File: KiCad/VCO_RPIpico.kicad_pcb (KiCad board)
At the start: 2 copper layers, 138 x 83 mm, 92 parts, among them J1 AudioJack, J2 Power Jack, SW1 LFO1/2, SW2 Select LFO WaveForm, SW3 Fire4, SW4 Fire3, SW5 Fire2, SW6 Fire1, SW7 Shift2/Save, SW8 Shift1 / Select Bank, U2 PT2399, U3 L7805, sw10 sw_led_fire2, sw11 sw_led_fire3, sw12 sw_led_fire4, sw9 sw_led_fire1

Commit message: KiCad: Schaltplan angepasst
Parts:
- removed R1: 1k, Resistor_SMD:R_1206_3216Metric
- removed R13, R14, R15: 100k, Potentiometer_THT:Potentiometer_Alps_RK09K_Single_Vertical
- added C24: 220n, Capacitor_SMD:C_1206_3216Metric, B.Cu at (103.0, 70.3)
- added R30: 10k, Resistor_SMD:R_1206_3216Metric, F.Cu at (135.0, 39.8)
- added RV1: 10k, poti_alps:Potentiometer_Alps_RK09K_Single_Vertical, F.Cu at (54.5, 71.5)
- added RV2: 10k, poti_alps:Potentiometer_Alps_RK09K_Single_Vertical, F.Cu at (54.5, 101.5)
- added RV3: 10k, poti_alps:Potentiometer_Alps_RK09K_Single_Vertical, F.Cu at (90.5, 101.5)
- C13: value 82nF -> 68nF
- J1: value AudioJack -> AudioJack3_Ground; footprint Connector_Audio:Jack_3.5mm_Ledino_KB3SPRS_Horizontal -> Audiosockets:Jack_3.5mm_Ledino_KB3SPRS_Horizontal
- R19: value 10k -> 4,7k
- RV4, RV5: footprint Potentiometer_THT:Potentiometer_Alps_RK09K_Single_Vertical -> poti_alps:Potentiometer_Alps_RK09K_Single_Vertical
- RV6: value 100k -> 50k; footprint Potentiometer_THT:Potentiometer_Alps_RK09K_Single_Vertical -> poti_alps:Potentiometer_Alps_RK09K_Single_Vertical
- moved R28 18.8 mm to (97.9, 41.1)
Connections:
- J1 pad R: (no net) -> Net-(J1-PadR)
- J1 pad S: Net-(J1-PadS) -> GND
- J1 pad T: GND -> Net-(J1-PadT)
- RV6 pad 2: Net-(J1-PadS) -> Net-(J1-PadT)
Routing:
- net Net-(J1-PadS): track 28.6 -> 0.00 mm
- net Net-(J1-PadT): track 0.00 -> 25.8 mm
- net Net-(C21-Pad2): track 97.9 -> 79.3 mm
- net +3V3: track 103.3 -> 85.1 mm
- net Net-(R5-Pad2): track 14.9 -> 0.00 mm
- net Net-(R4-Pad2): track 14.9 -> 0.10 mm
- net GND: track 145.4 -> 133.0 mm
- net Net-(R28-Pad1): track 12.2 -> 0.00 mm, vias 1 -> 0
- net Net-(C17-Pad2): track 78.7 -> 73.4 mm, vias 2 -> 1
- net Net-(R19-Pad1): track 5.15 -> 0.00 mm
- net Net-(R6-Pad2): track 3.01 -> 0.00 mm
- net Net-(C23-Pad2): track 3.67 -> 1.27 mm

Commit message: KiCad änderungen
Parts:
- removed D12, D16: LED Fire1, LED_SMD:LED_1206_3216Metric
- removed D13, D17: LED Fire2, LED_SMD:LED_1206_3216Metric
- removed D14, D18: LED Fire3, LED_SMD:LED_1206_3216Metric
- removed D15, D19: LED Fire4, LED_SMD:LED_1206_3216Metric
- removed sw10: sw_led_fire2, switches:Multimec Switch THT
- removed sw11: sw_led_fire3, switches:Multimec Switch THT
- removed sw12: sw_led_fire4, switches:Multimec Switch THT
- removed sw9: sw_led_fire1, switches:Multimec Switch THT
- D1: value LED LFO2 -> LED LFO2 yel
- D2: value LED LFO1 -> LED LFO1 yel
- D3: value LED Shift1 -> LED Shift1 yel
- D4: value LED Fire1 -> LED Fire1 blu
- D5: value LED Fire2 -> LED Fire2 blu
- D6: value LED Fire3 -> LED Fire3 blu
- D7: value LED Fire4 -> LED Fire4 blu
- D9: value LED Shift2 -> LED Save red
- J1: footprint Audiosockets:Jack_3.5mm_Ledino_KB3SPRS_Horizontal -> Connector_Audio:Jack_6.35mm_Neutrik_NMJ6HFD2_Horizontal
- R30: moved to B.Cu
- moved D20 49.8 mm to (165.0, 52.6), turned to 0 degrees
- moved R30 47.9 mm to (174.5, 67.0), turned to 180 degrees
- moved J1 47.1 mm to (103.9, 73.9), turned to 90 degrees
- moved R28 42.8 mm to (130.6, 68.8)
- moved RV4 36.0 mm to (90.5, 71.5)
- moved RV5 36.0 mm to (126.5, 71.5)
- moved J2 35.9 mm to (153.2, 61.8)
- moved C10 12.6 mm to (122.7, 53.6)
- moved C24 3.98 mm to (99.8, 72.7), turned to 90 degrees
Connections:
- RV4 pad 2: GND -> Net-(R19-Pad1)
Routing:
- net +5C: track 141.0 -> 79.4 mm
- net Net-(C17-Pad2): track 73.4 -> 38.4 mm
- net Net-(C21-Pad2): track 79.3 -> 45.7 mm
- net /Wave_out: track 82.2 -> 52.1 mm, vias 2 -> 1
- net /led_fire1: track 26.3 -> 2.29 mm
- net /led_fire2: track 26.8 -> 3.06 mm
- net +3V3: track 85.1 -> 63.1 mm
- net Net-(J1-PadT): track 25.8 -> 10.5 mm
- net Net-(D20-K): track 30.0 -> 18.1 mm
- net /led_fire3: track 27.8 -> 19.9 mm
- net Net-(A1-GPIO5): track 19.8 -> 14.5 mm
- net Net-(D20-A): track 5.27 -> 0.00 mm
- net /sw_fire1: track 40.8 -> 38.6 mm
- net /sw_fire2: track 54.3 -> 52.1 mm
- net /sw_fire3: track 92.5 -> 90.3 mm
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
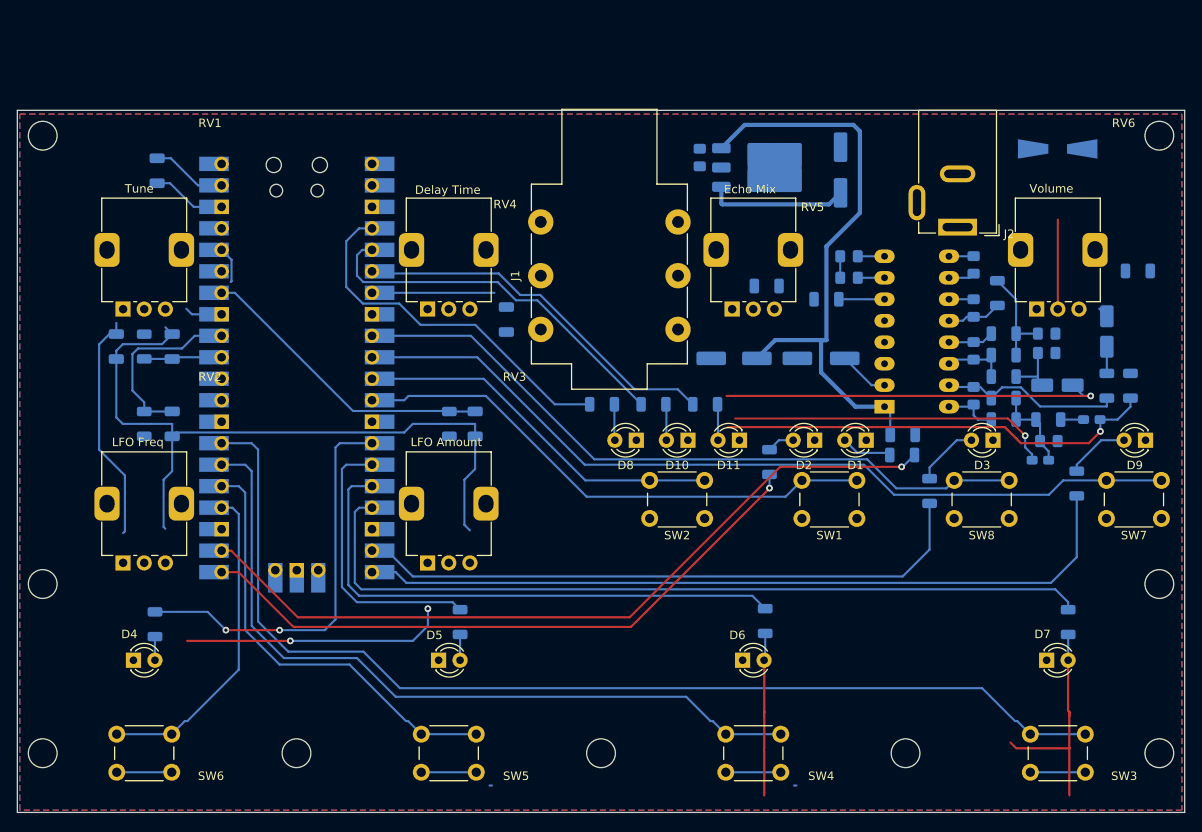
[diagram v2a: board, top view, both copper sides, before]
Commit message: PCB correctur
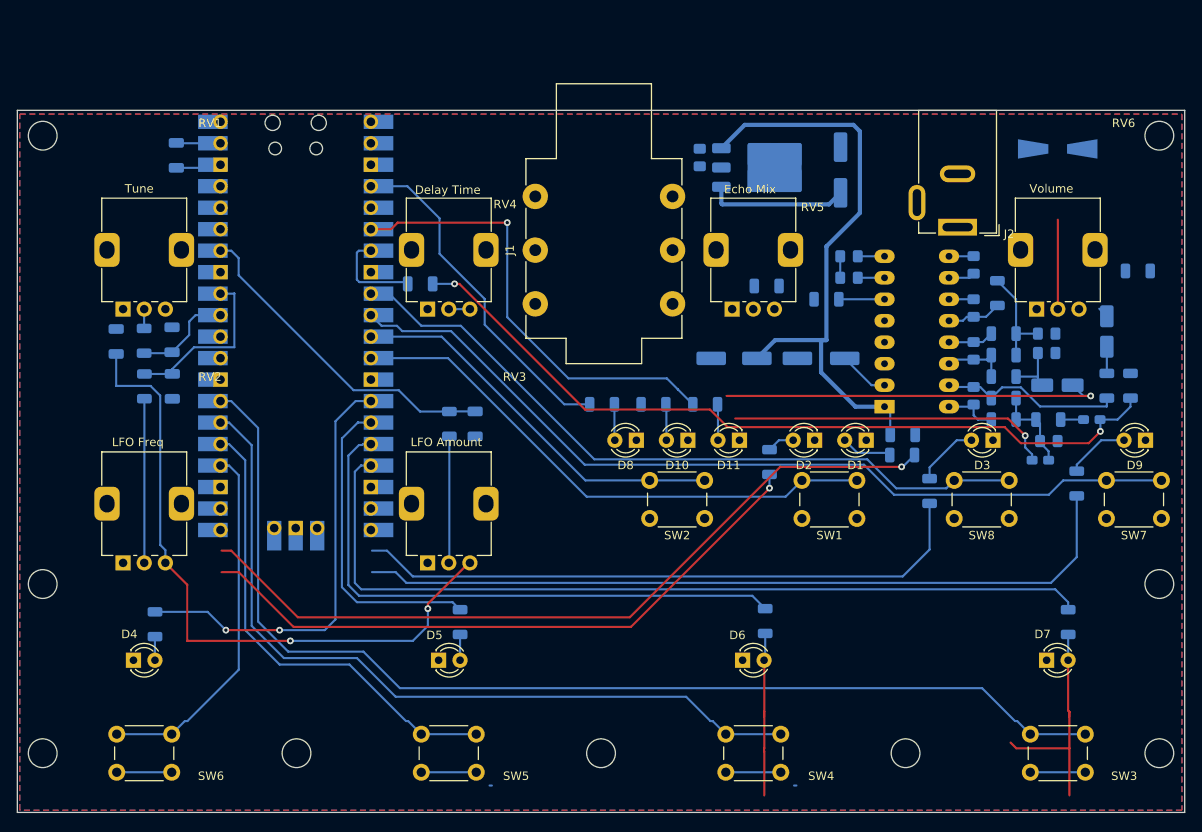
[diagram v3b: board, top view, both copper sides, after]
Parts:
- moved C24 11.0 mm to (89.6, 68.5), turned to 180 degrees
- moved A1 4.98 mm to (74.9, 73.5)
- moved C3 4.44 mm to (60.3, 80.6)
- moved R5 4.44 mm to (57.0, 80.6)
- moved J1 3.09 mm to (103.2, 70.9)
- moved C5 2.91 mm to (60.8, 53.3)
- moved C4 0.80 mm to (60.3, 75.1)
- moved R6 0.68 mm to (57.0, 75.2)
- moved C6 0.60 mm to (53.7, 75.3), turned to -90 degrees
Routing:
- net GND: track 132.2 -> 40.0 mm
- net Net-(A1-GPIO3): track 44.4 -> 0.04 mm
- net /Wave_out: track 52.1 -> 94.0 mm, vias 1 -> 2
- net Net-(R5-Pad2): track 0.00 -> 19.4 mm
- net +3V3: track 63.1 -> 78.7 mm
- net Net-(R4-Pad2): track 0.10 -> 15.1 mm
- net Net-(A1-GPIO4): track 44.4 -> 53.9 mm, vias 0 -> 1
- net /sw_fire1: track 38.6 -> 43.5 mm
- net Net-(A1-GPIO13): track 96.8 -> 101.5 mm
- net Net-(A1-GPIO10): track 47.6 -> 52.1 mm
- net /sw_fire2: track 52.1 -> 56.5 mm
- net Net-(A1-GPIO12): track 64.7 -> 69.0 mm
- net Net-(A1-GPIO11): track 32.8 -> 36.9 mm
- net /sw_fire3: track 90.3 -> 94.3 mm
- net /sw_fire4: track 128.6 -> 132.3 mm
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
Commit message: PCB correctur
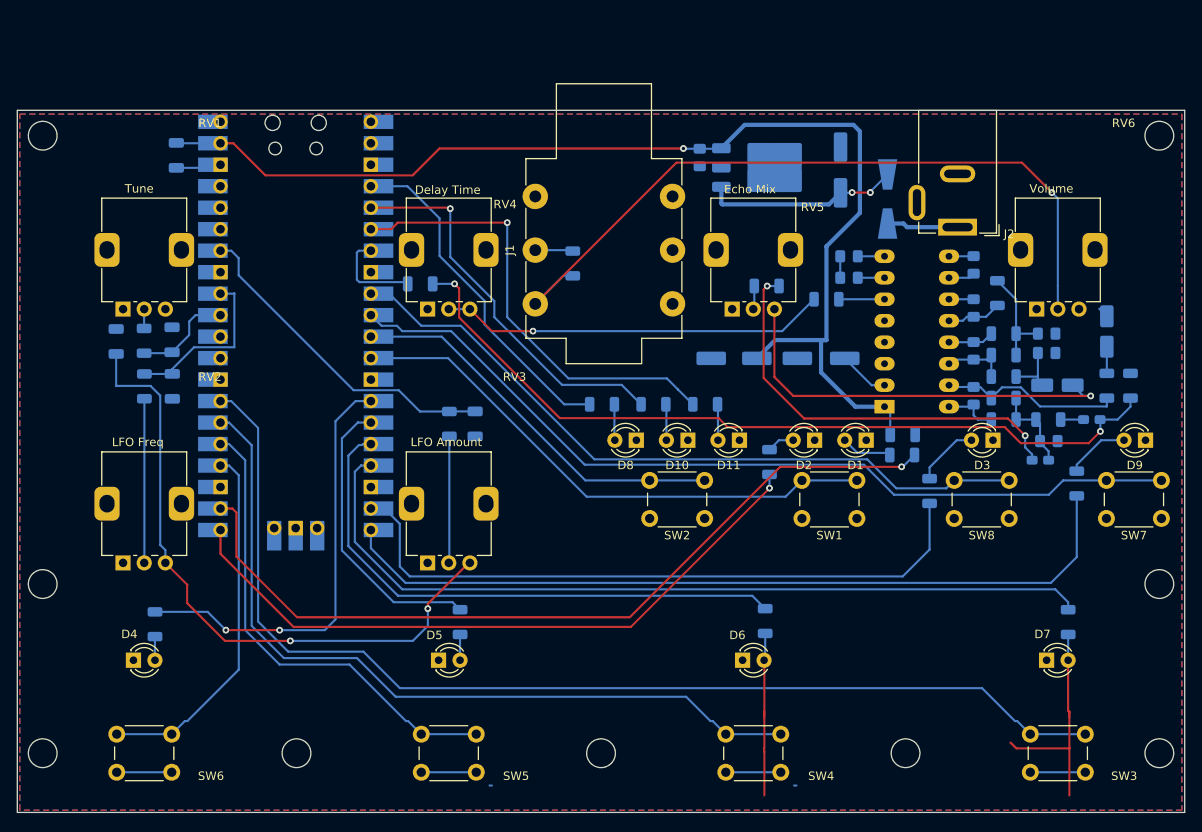
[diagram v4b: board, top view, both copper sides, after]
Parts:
- moved R30 66.8 mm to (107.7, 66.1), turned to -90 degrees
- moved D20 21.0 mm to (144.9, 58.5), turned to -90 degrees
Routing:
- net Net-(J1-PadT): track 10.5 -> 89.3 mm, vias 0 -> 1
- net +5C: track 75.8 -> 137.9 mm, vias 0 -> 1
- net Net-(A1-GPIO3): track 0.04 -> 46.1 mm, vias 0 -> 1
- net Net-(R19-Pad1): track 2.71 -> 46.2 mm, vias 0 -> 1
- net Net-(C17-Pad2): track 38.4 -> 49.4 mm, vias 1 -> 2
- net Net-(D20-A): track 0.00 -> 8.46 mm
- net Net-(D20-K): track 18.1 -> 24.6 mm, vias 0 -> 2
- net Net-(A1-GPIO17): track 93.1 -> 98.4 mm
- net Net-(A1-GPIO14): track 74.0 -> 79.1 mm
- net Net-(J1-PadR): track 0.00 -> 4.48 mm
- net Net-(A1-GPIO16): track 75.9 -> 79.7 mm
- net Net-(A1-GPIO15): track 92.3 -> 95.8 mm
- net Net-(C21-Pad2): track 45.7 -> 49.0 mm
- net Net-(A1-GPIO13): track 101.5 -> 98.7 mm
- net Net-(R28-Pad1): track 0.00 -> 2.78 mm
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
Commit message: korrektur 260330
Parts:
- moved D20 4.73 mm to (145.4, 53.8)
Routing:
- net +3V3: track 76.1 -> 105.5 mm, vias 2 -> 3
- net /led_fire4: track 27.7 -> 3.81 mm
- net /led_fire3: track 19.9 -> 3.27 mm
- net Net-(C21-Pad2): track 49.0 -> 40.0 mm
- net +5C: track 137.9 -> 130.7 mm
- net Net-(J1-PadT): track 89.3 -> 83.8 mm
- net Net-(D20-A): track 8.46 -> 11.8 mm
- net Net-(D20-K): track 24.6 -> 27.8 mm, vias 2 -> 0
- net Net-(C17-Pad2): track 49.4 -> 46.7 mm
- net GND: vias 0 -> 47
